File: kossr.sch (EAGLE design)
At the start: 18 parts, among them T1 BTA12-600, U1 TINY45-20-DIP

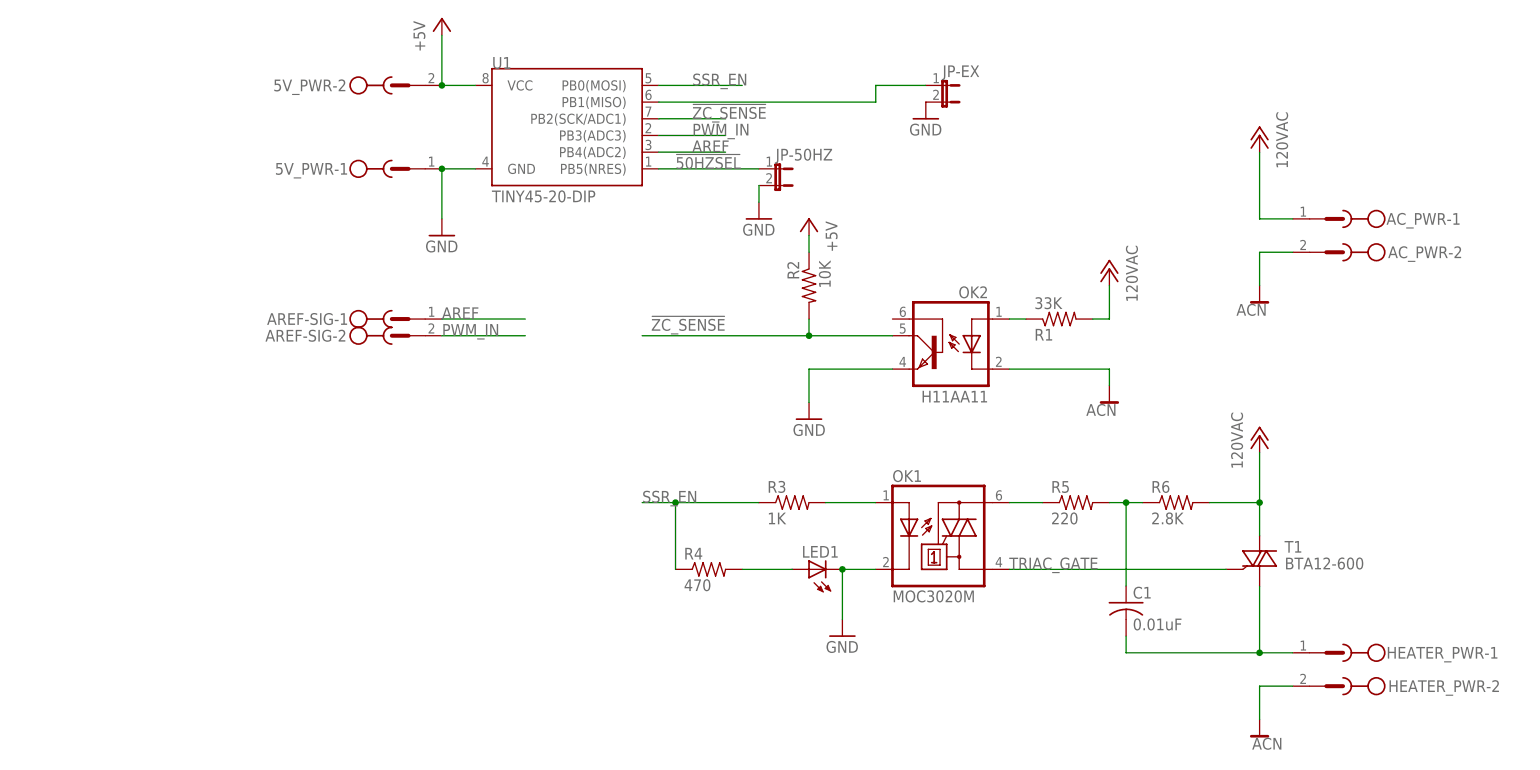
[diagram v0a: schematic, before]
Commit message: update to kossr 0.2
adds input r/c filter
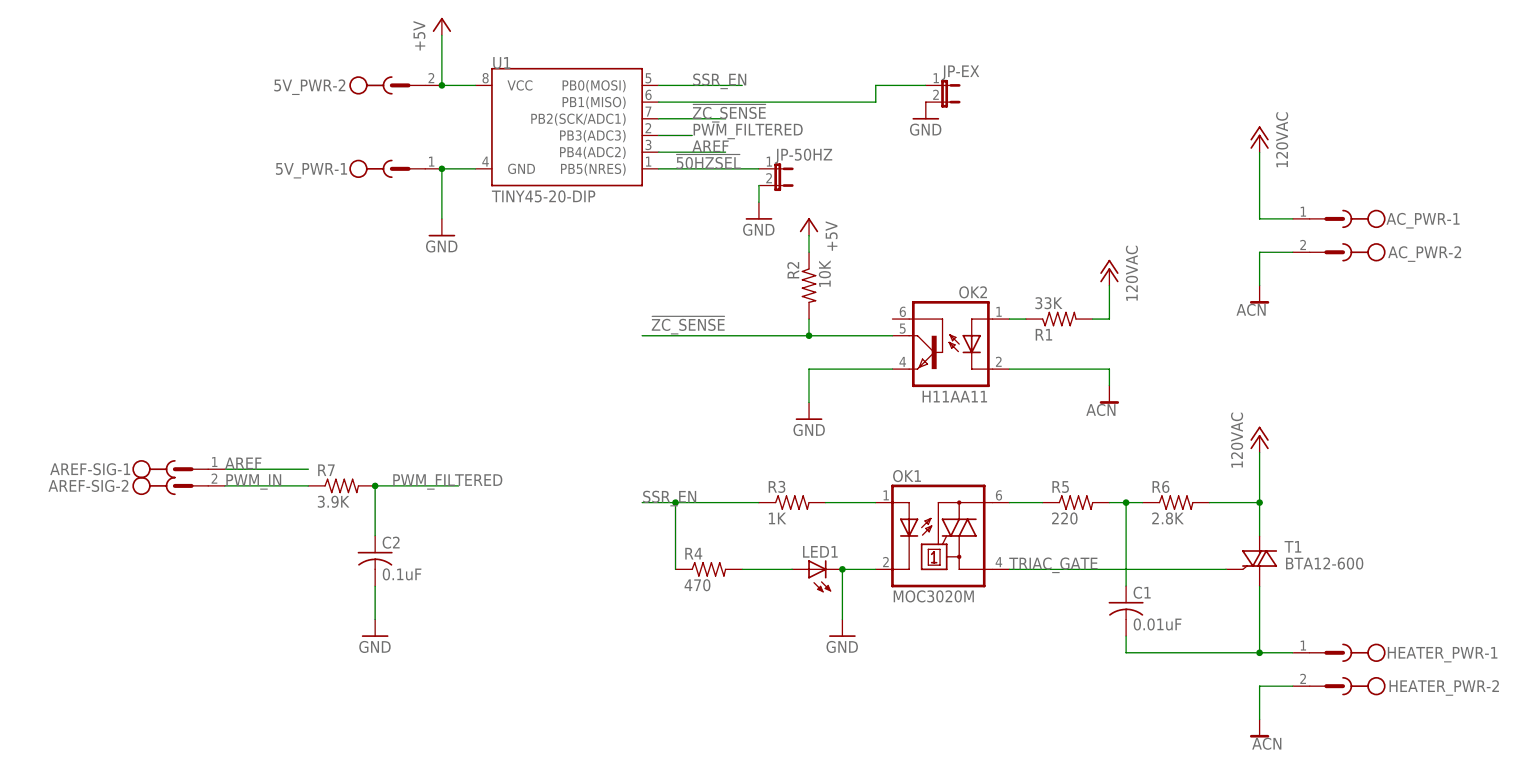
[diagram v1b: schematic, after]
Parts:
- added C2: 0.1uF, adafruit:C-US025-024X044
- added R7: 3.9K, rcl:R-US_0207/7
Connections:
- new net PWM_FILTERED: C2.1, R7.2, U1.PB3(ADC3)
- net GND: now also C2.2
- net PWM_IN: now also R7.1; no longer U1.PB3(ADC3)
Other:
- moved on the sheet: AREF-SIG-1, AREF-SIG-2
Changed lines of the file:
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@@
 <?xml version="1.0" encoding="utf-8"?>
 <!DOCTYPE eagle SYSTEM "eagle.dtd">
-<eagle version="6.3">
+<eagle version="6.6.0">
 <drawing>
 <settings>
@@
 <part name="JP-EX" library="SparkFun-Retired" deviceset="JUMPER-2" device="SMD-NO"/>
 <part name="GND5" library="supply1" deviceset="GND" device=""/>
+<part name="C2" library="adafruit" deviceset="C-US" device="025-024X044" value="0.1uF"/>
+<part name="R7" library="rcl" deviceset="R-US_" device="0207/7" value="3.9K"/>
+<part name="GND6" library="supply1" deviceset="GND" device=""/>
 </parts>
 <sheets>
@@
 <instance part="5V_PWR" gate="-1" x="-10.16" y="93.98"/>
 <instance part="5V_PWR" gate="-2" x="-10.16" y="106.68"/>
-<instance part="AREF-SIG" gate="-1" x="-10.16" y="71.12" rot="MR180"/>
-<instance part="AREF-SIG" gate="-2" x="-10.16" y="68.58" rot="MR180"/>
+<instance part="AREF-SIG" gate="-1" x="-43.18" y="48.26" rot="MR180"/>
+<instance part="AREF-SIG" gate="-2" x="-43.18" y="45.72" rot="MR180"/>
 <instance part="HEATER_PWR" gate="-1" x="134.62" y="20.32" rot="MR0"/>
 <instance part="HEATER_PWR" gate="-2" x="134.62" y="15.24" rot="MR0"/>
@@
 <instance part="JP-EX" gate="A" x="73.66" y="106.68" rot="R270"/>
 <instance part="GND5" gate="1" x="71.12" y="101.6"/>
+<instance part="C2" gate="G$1" x="-12.7" y="35.56"/>
+<instance part="R7" gate="G$1" x="-17.78" y="45.72"/>
+<instance part="GND6" gate="1" x="-12.7" y="22.86"/>
 </instances>
 <busses>
@@
 <pinref part="JP-EX" gate="A" pin="2"/>
 <pinref part="GND5" gate="1" pin="GND"/>
+</segment>
+<segment>
+<pinref part="C2" gate="G$1" pin="2"/>
+<pinref part="GND6" gate="1" pin="GND"/>
+<wire x1="-12.7" y1="25.4" x2="-12.7" y2="30.48" width="0.1524" layer="91"/>
 </segment>
 </net>
@@
 <segment>
 <pinref part="AREF-SIG" gate="-1" pin="SK"/>
-<wire x1="-2.54" y1="71.12" x2="10.16" y2="71.12" width="0.1524" layer="91"/>
-<label x="-2.54" y="71.12" size="1.778" layer="95"/>
+<wire x1="-35.56" y1="48.26" x2="-22.86" y2="48.26" width="0.1524" layer="91"/>
+<label x="-35.56" y="48.26" size="1.778" layer="95"/>
 </segment>
 <segment>
@@
 <segment>
 <pinref part="AREF-SIG" gate="-2" pin="SK"/>
-<wire x1="-2.54" y1="68.58" x2="10.16" y2="68.58" width="0.1524" layer="91"/>
-<label x="-2.54" y="68.58" size="1.778" layer="95"/>
-</segment>
-<segment>
-<pinref part="U1" gate="G$1" pin="PB3(ADC3)"/>
-<wire x1="30.48" y1="99.06" x2="40.64" y2="99.06" width="0.1524" layer="91"/>
-<label x="35.56" y="99.06" size="1.778" layer="95"/>
+<wire x1="-35.56" y1="45.72" x2="-22.86" y2="45.72" width="0.1524" layer="91"/>
+<label x="-35.56" y="45.72" size="1.778" layer="95"/>
+<pinref part="R7" gate="G$1" pin="1"/>
 </segment>
 </net>
@@
 </segment>
 </net>
+<net name="PWM_FILTERED" class="0">
+<segment>
+<pinref part="C2" gate="G$1" pin="1"/>
+<pinref part="R7" gate="G$1" pin="2"/>
+<wire x1="-12.7" y1="38.1" x2="-12.7" y2="45.72" width="0.1524" layer="91"/>
+<wire x1="-12.7" y1="45.72" x2="0" y2="45.72" width="0.1524" layer="91"/>
+<junction x="-12.7" y="45.72"/>
+<label x="-10.16" y="45.72" size="1.778" layer="95"/>
+</segment>
+<segment>
+<pinref part="U1" gate="G$1" pin="PB3(ADC3)"/>
+<wire x1="30.48" y1="99.06" x2="35.56" y2="99.06" width="0.1524" layer="91"/>
+<label x="35.56" y="99.06" size="1.778" layer="95"/>
+</segment>
+</net>
